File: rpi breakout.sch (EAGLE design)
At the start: 48 parts, among them IC1 PCA9505, J1 RASPBERRYPI-40-PIN-GPIO_PTH, U1 MAX11642EEG, U2 MAX11642EEG, U3 MAX11642EEG

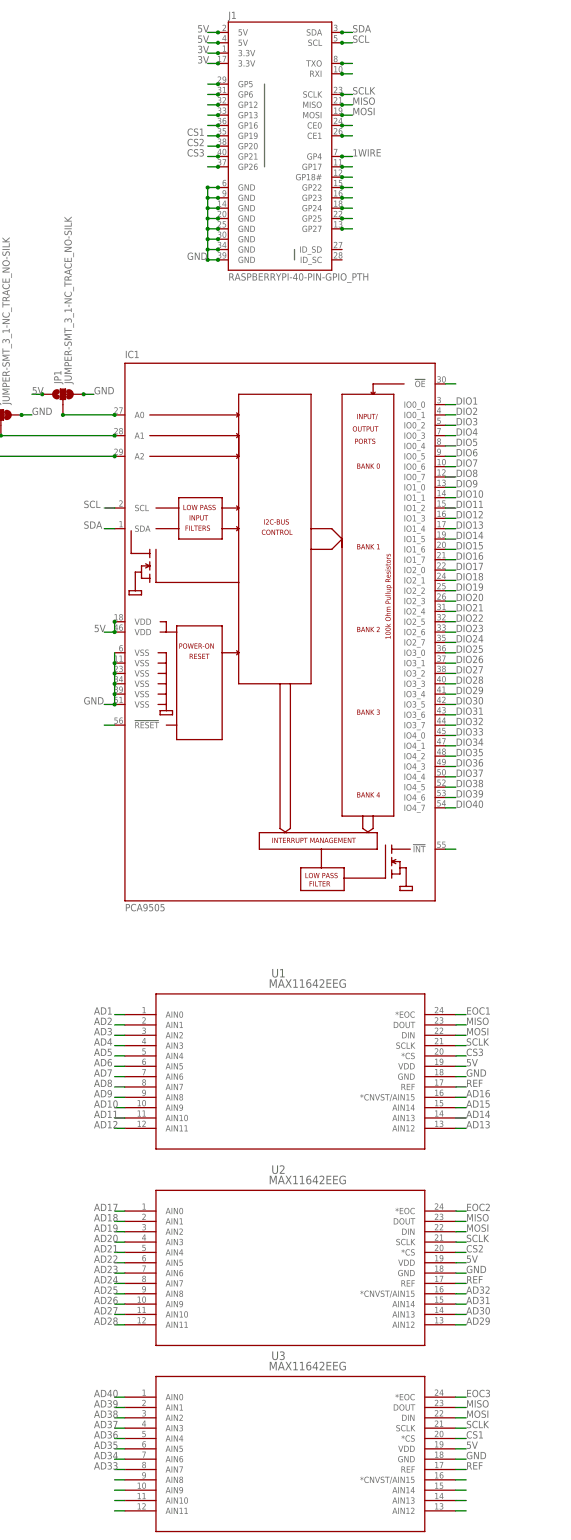
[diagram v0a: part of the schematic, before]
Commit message: FInal routing pass
connected remaining pins, added decoupling caps to AREF pins.
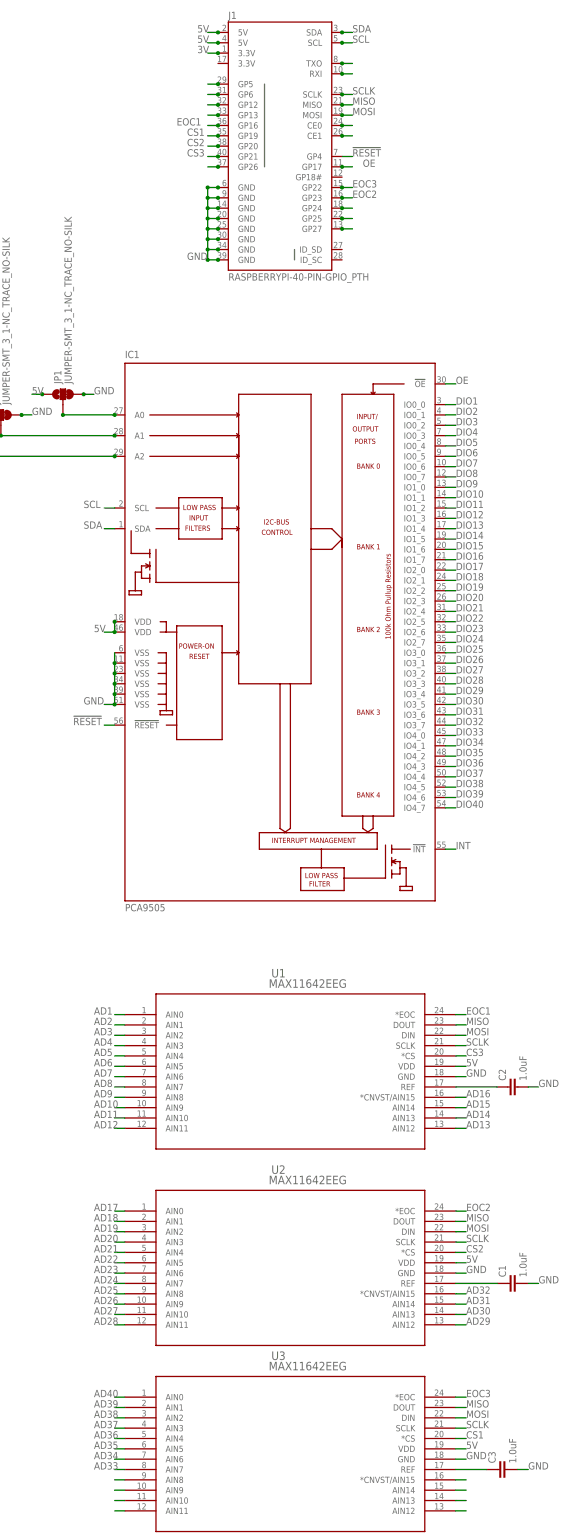
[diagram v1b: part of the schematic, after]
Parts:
- added C1, C2, C3: 1.0uF, SparkFun-Capacitors:1.0UF-0805-25V-10%
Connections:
- net N$14 renamed INT
- removed net 1WIRE: J1.GP4
- removed net N$1: IC1.!RESET
- removed net N$15: IC1.!OE
- removed net N$32: J1.GP17
- removed net N$33: J1.GP18#
- removed net N$34: J1.GP22
- removed net N$35: J1.GP23
- removed net N$9: J1.GP16
- removed net REF: U1.REF, U2.REF, U3.REF
- new net !RESET: IC1.!RESET, J1.GP4
- new net N$11: C2.1, U1.REF
- new net N$2: C3.1, U3.REF
- new net N$3: C1.1, U2.REF
- new net OE: IC1.!OE, J1.GP17
- net 3V: no longer J1.3.3V@17
- net EOC1: now also J1.GP16
- net EOC2: now also J1.GP23
- net EOC3: now also J1.GP22
- net GND: now also C1.2, C2.2, C3.2
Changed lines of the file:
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@@
 <part name="JP2" library="SparkFun-Jumpers" library_urn="urn:adsk.eagle:library:528" deviceset="JUMPER-SMT_3_1-NC_TRACE" device="_NO-SILK" package3d_urn="urn:adsk.eagle:package:39287/1"/>
 <part name="JP3" library="SparkFun-Jumpers" library_urn="urn:adsk.eagle:library:528" deviceset="JUMPER-SMT_3_1-NC_TRACE" device="_NO-SILK" package3d_urn="urn:adsk.eagle:package:39287/1"/>
+<part name="C1" library="SparkFun-Capacitors" library_urn="urn:adsk.eagle:library:510" deviceset="1.0UF" device="-0805-25V-10%" package3d_urn="urn:adsk.eagle:package:37429/1" value="1.0uF"/>
+<part name="C2" library="SparkFun-Capacitors" library_urn="urn:adsk.eagle:library:510" deviceset="1.0UF" device="-0805-25V-10%" package3d_urn="urn:adsk.eagle:package:37429/1" value="1.0uF"/>
+<part name="C3" library="SparkFun-Capacitors" library_urn="urn:adsk.eagle:library:510" deviceset="1.0UF" device="-0805-25V-10%" package3d_urn="urn:adsk.eagle:package:37429/1" value="1.0uF"/>
 </parts>
 <sheets>
@@
 <attribute name="VALUE" x="175.641" y="83.82" size="1.778" layer="96" font="vector" rot="R90" align="top-left"/>
 </instance>
+<instance part="C1" gate="G$1" x="317.5" y="-127" smashed="yes" rot="R90">
+<attribute name="NAME" x="314.579" y="-125.476" size="1.778" layer="95" font="vector" rot="R90"/>
+<attribute name="VALUE" x="319.659" y="-125.476" size="1.778" layer="96" font="vector" rot="R90"/>
+</instance>
+<instance part="C2" gate="G$1" x="317.5" y="-78.74" smashed="yes" rot="R90">
+<attribute name="NAME" x="314.579" y="-77.216" size="1.778" layer="95" font="vector" rot="R90"/>
+<attribute name="VALUE" x="319.659" y="-77.216" size="1.778" layer="96" font="vector" rot="R90"/>
+</instance>
+<instance part="C3" gate="G$1" x="314.96" y="-172.72" smashed="yes" rot="R90">
+<attribute name="NAME" x="312.039" y="-171.196" size="1.778" layer="95" font="vector" rot="R90"/>
+<attribute name="VALUE" x="317.119" y="-171.196" size="1.778" layer="96" font="vector" rot="R90"/>
+</instance>
 </instances>
 <busses>
@@
 </segment>
 </net>
-<net name="N$9" class="0">
-<segment>
-<pinref part="J1" gate="G$1" pin="GP16"/>
-<wire x1="243.84" y1="157.48" x2="241.3" y2="157.48" width="0.1524" layer="91"/>
-<junction x="243.84" y="157.48"/>
-</segment>
-</net>
 <net name="N$13" class="0">
 <segment>
@@
 </segment>
 </net>
-<net name="N$32" class="0">
-<segment>
-<pinref part="J1" gate="G$1" pin="GP17"/>
-<wire x1="274.32" y1="147.32" x2="276.86" y2="147.32" width="0.1524" layer="91"/>
-<junction x="274.32" y="147.32"/>
-</segment>
-</net>
-<net name="N$33" class="0">
-<segment>
-<pinref part="J1" gate="G$1" pin="GP18#"/>
-<wire x1="274.32" y1="144.78" x2="276.86" y2="144.78" width="0.1524" layer="91"/>
-<junction x="274.32" y="144.78"/>
-</segment>
-</net>
-<net name="N$34" class="0">
-<segment>
-<pinref part="J1" gate="G$1" pin="GP22"/>
-<wire x1="274.32" y1="142.24" x2="276.86" y2="142.24" width="0.1524" layer="91"/>
-<junction x="274.32" y="142.24"/>
-</segment>
-</net>
-<net name="N$35" class="0">
-<segment>
-<pinref part="J1" gate="G$1" pin="GP23"/>
-<wire x1="274.32" y1="139.7" x2="276.86" y2="139.7" width="0.1524" layer="91"/>
-<junction x="274.32" y="139.7"/>
-</segment>
-</net>
 <net name="N$36" class="0">
 <segment>
@@
 <junction x="243.84" y="175.26"/>
 <label x="238.76" y="175.26" size="1.778" layer="95"/>
-</segment>
-<segment>
-<pinref part="J1" gate="G$1" pin="3.3V@17"/>
-<wire x1="243.84" y1="172.72" x2="241.3" y2="172.72" width="0.1524" layer="91"/>
-<junction x="243.84" y="172.72"/>
-<label x="238.76" y="172.72" size="1.778" layer="95"/>
-</segment>
-</net>
-<net name="1WIRE" class="0">
-<segment>
-<pinref part="J1" gate="G$1" pin="GP4"/>
-<wire x1="274.32" y1="149.86" x2="276.86" y2="149.86" width="0.1524" layer="91"/>
-<junction x="274.32" y="149.86"/>
-<label x="276.86" y="149.86" size="1.778" layer="95"/>
 </segment>
 </net>
@@
 <junction x="180.34" y="81.28"/>
 </segment>
+<segment>
+<pinref part="C2" gate="G$1" pin="2"/>
+<wire x1="320.04" y1="-78.74" x2="322.58" y2="-78.74" width="0.1524" layer="91"/>
+<label x="322.58" y="-78.74" size="1.778" layer="95"/>
+</segment>
+<segment>
+<pinref part="C1" gate="G$1" pin="2"/>
+<wire x1="320.04" y1="-127" x2="322.58" y2="-127" width="0.1524" layer="91"/>
+<label x="322.58" y="-127" size="1.778" layer="95"/>
+</segment>
+<segment>
+<pinref part="C3" gate="G$1" pin="2"/>
+<wire x1="317.5" y1="-172.72" x2="320.04" y2="-172.72" width="0.1524" layer="91"/>
+<label x="320.04" y="-172.72" size="1.778" layer="95"/>
+</segment>
 </net>
 <net name="5V" class="0">
@@
 </segment>
 </net>
-<net name="N$1" class="0">
+<net name="!RESET" class="0">
 <segment>
 <pinref part="IC1" gate="G$1" pin="!RESET"/>
 <wire x1="218.44" y1="10.16" x2="215.9" y2="10.16" width="0.1524" layer="91"/>
-</segment>
-</net>
-<net name="N$14" class="0">
+<label x="208.28" y="10.16" size="1.778" layer="95"/>
+</segment>
+<segment>
+<pinref part="J1" gate="G$1" pin="GP4"/>
+<wire x1="274.32" y1="149.86" x2="276.86" y2="149.86" width="0.1524" layer="91"/>
+<label x="276.86" y="149.86" size="1.778" layer="95"/>
+</segment>
+</net>
+<net name="INT" class="0">
 <segment>
 <pinref part="IC1" gate="G$1" pin="!INT"/>
 <wire x1="299.72" y1="-20.32" x2="302.26" y2="-20.32" width="0.1524" layer="91"/>
-</segment>
-</net>
-<net name="N$15" class="0">
+<label x="302.26" y="-20.32" size="1.778" layer="95"/>
+</segment>
+</net>
+<net name="OE" class="0">
 <segment>
 <pinref part="IC1" gate="G$1" pin="!OE"/>
 <wire x1="299.72" y1="93.98" x2="302.26" y2="93.98" width="0.1524" layer="91"/>
+<label x="302.26" y="93.98" size="1.778" layer="95"/>
+</segment>
+<segment>
+<pinref part="J1" gate="G$1" pin="GP17"/>
+<wire x1="274.32" y1="147.32" x2="276.86" y2="147.32" width="0.1524" layer="91"/>
+<junction x="274.32" y="147.32"/>
+<label x="279.4" y="147.32" size="1.778" layer="95"/>
 </segment>
 </net>
@@
 </segment>
 </net>
-<net name="REF" class="0">
-<segment>
-<pinref part="U1" gate="A" pin="REF"/>
-<wire x1="302.26" y1="-78.74" x2="304.8" y2="-78.74" width="0.1524" layer="91"/>
-<label x="304.8" y="-78.74" size="1.778" layer="95"/>
-</segment>
-<segment>
-<pinref part="U2" gate="A" pin="REF"/>
-<wire x1="302.26" y1="-127" x2="304.8" y2="-127" width="0.1524" layer="91"/>
-<label x="304.8" y="-127" size="1.778" layer="95"/>
-</segment>
-<segment>
-<pinref part="U3" gate="A" pin="REF"/>
-<wire x1="302.26" y1="-172.72" x2="304.8" y2="-172.72" width="0.1524" layer="91"/>
-<label x="304.8" y="-172.72" size="1.778" layer="95"/>
-</segment>
-</net>
 <net name="EOC1" class="0">
 <segment>
@@
 <label x="304.8" y="-60.96" size="1.778" layer="95"/>
 </segment>
+<segment>
+<pinref part="J1" gate="G$1" pin="GP16"/>
+<wire x1="243.84" y1="157.48" x2="241.3" y2="157.48" width="0.1524" layer="91"/>
+<junction x="243.84" y="157.48"/>
+<label x="233.68" y="157.48" size="1.778" layer="95"/>
+</segment>
 </net>
 <net name="EOC2" class="0">
@@
 <wire x1="302.26" y1="-109.22" x2="304.8" y2="-109.22" width="0.1524" layer="91"/>
 <label x="304.8" y="-109.22" size="1.778" layer="95"/>
+</segment>
+<segment>
+<pinref part="J1" gate="G$1" pin="GP23"/>
+<wire x1="274.32" y1="139.7" x2="276.86" y2="139.7" width="0.1524" layer="91"/>
+<junction x="274.32" y="139.7"/>
+<label x="276.86" y="139.7" size="1.778" layer="95"/>
 </segment>
 </net>
@@
 <label x="304.8" y="-154.94" size="1.778" layer="95"/>
 </segment>
+<segment>
+<pinref part="J1" gate="G$1" pin="GP22"/>
+<wire x1="274.32" y1="142.24" x2="276.86" y2="142.24" width="0.1524" layer="91"/>
+<junction x="274.32" y="142.24"/>
+<label x="276.86" y="142.24" size="1.778" layer="95"/>
+</segment>
 </net>
 <net name="CS3" class="0">
@@
 </segment>
 </net>
+<net name="N$2" class="0">
+<segment>
+<pinref part="U3" gate="A" pin="REF"/>
+<pinref part="C3" gate="G$1" pin="1"/>
+<wire x1="302.26" y1="-172.72" x2="309.88" y2="-172.72" width="0.1524" layer="91"/>
+</segment>
+</net>
+<net name="N$3" class="0">
+<segment>
+<pinref part="U2" gate="A" pin="REF"/>
+<pinref part="C1" gate="G$1" pin="1"/>
+<wire x1="302.26" y1="-127" x2="312.42" y2="-127" width="0.1524" layer="91"/>
+</segment>
+</net>
+<net name="N$11" class="0">
+<segment>
+<pinref part="U1" gate="A" pin="REF"/>
+<pinref part="C2" gate="G$1" pin="1"/>
+<wire x1="302.26" y1="-78.74" x2="312.42" y2="-78.74" width="0.1524" layer="91"/>
+</segment>
+</net>

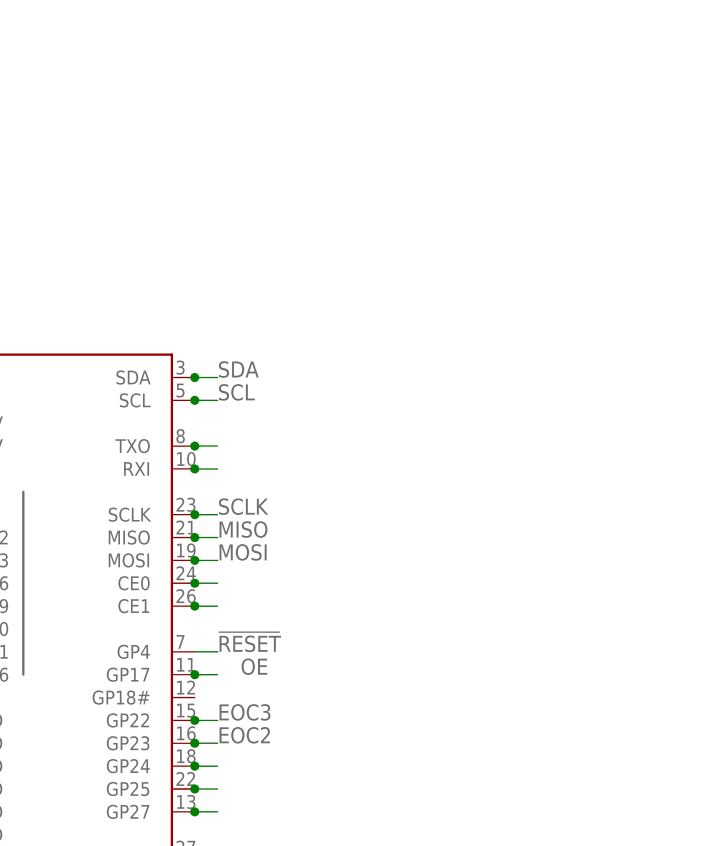
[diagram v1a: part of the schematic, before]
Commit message: pulled OE and Reset lines to 5v and ground
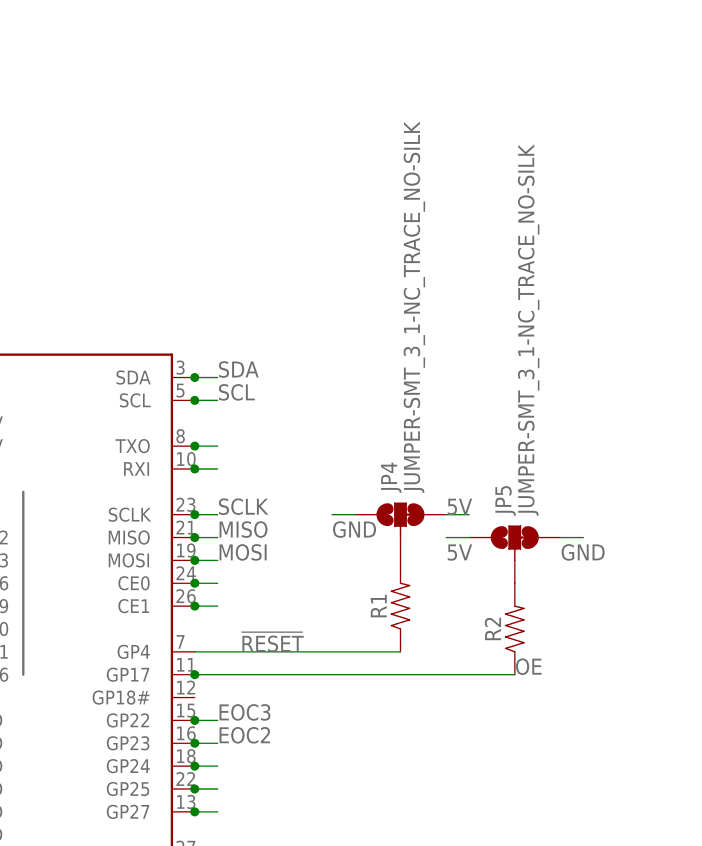
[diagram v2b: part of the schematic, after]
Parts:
- added JP4, JP5: JUMPER-SMT_3_1-NC_TRACE_NO-SILK, SparkFun-Jumpers:JUMPER-SMT_3_1-NC_TRACE_NO-SILK
- added R1, R2: (no value), SparkFun-Resistors:RESISTOR0805
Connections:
- new net N$1: JP4.2, R1.2
- new net N$4: JP5.2, R2.2
- net !RESET: now also R1.1
- net 5V: now also JP4.3, JP5.1
- net GND: now also JP4.1, JP5.3
- net OE: now also R2.1
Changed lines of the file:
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@@
 <part name="C2" library="SparkFun-Capacitors" library_urn="urn:adsk.eagle:library:510" deviceset="1.0UF" device="-0805-25V-10%" package3d_urn="urn:adsk.eagle:package:37429/1" value="1.0uF"/>
 <part name="C3" library="SparkFun-Capacitors" library_urn="urn:adsk.eagle:library:510" deviceset="1.0UF" device="-0805-25V-10%" package3d_urn="urn:adsk.eagle:package:37429/1" value="1.0uF"/>
+<part name="R1" library="SparkFun-Resistors" library_urn="urn:adsk.eagle:library:532" deviceset="RESISTOR" device="0805" package3d_urn="urn:adsk.eagle:package:39651/1" value=" "/>
+<part name="R2" library="SparkFun-Resistors" library_urn="urn:adsk.eagle:library:532" deviceset="RESISTOR" device="0805" package3d_urn="urn:adsk.eagle:package:39651/1" value=" "/>
+<part name="JP4" library="SparkFun-Jumpers" library_urn="urn:adsk.eagle:library:528" deviceset="JUMPER-SMT_3_1-NC_TRACE" device="_NO-SILK" package3d_urn="urn:adsk.eagle:package:39287/1"/>
+<part name="JP5" library="SparkFun-Jumpers" library_urn="urn:adsk.eagle:library:528" deviceset="JUMPER-SMT_3_1-NC_TRACE" device="_NO-SILK" package3d_urn="urn:adsk.eagle:package:39287/1"/>
 </parts>
 <sheets>
@@
 <attribute name="NAME" x="312.039" y="-171.196" size="1.778" layer="95" font="vector" rot="R90"/>
 <attribute name="VALUE" x="317.119" y="-171.196" size="1.778" layer="96" font="vector" rot="R90"/>
+</instance>
+<instance part="R1" gate="G$1" x="297.18" y="154.94" smashed="yes" rot="R90">
+<attribute name="NAME" x="295.656" y="154.94" size="1.778" layer="95" font="vector" rot="R90" align="bottom-center"/>
+<attribute name="VALUE" x="298.704" y="154.94" size="1.778" layer="96" font="vector" rot="R90" align="top-center"/>
+</instance>
+<instance part="R2" gate="G$1" x="309.88" y="152.4" smashed="yes" rot="R90">
+<attribute name="NAME" x="308.356" y="152.4" size="1.778" layer="95" font="vector" rot="R90" align="bottom-center"/>
+<attribute name="VALUE" x="311.404" y="152.4" size="1.778" layer="96" font="vector" rot="R90" align="top-center"/>
+</instance>
+<instance part="JP4" gate="G$1" x="297.18" y="165.1" smashed="yes" rot="R90">
+<attribute name="NAME" x="296.799" y="167.64" size="1.778" layer="95" font="vector" rot="R90"/>
+<attribute name="VALUE" x="297.561" y="167.64" size="1.778" layer="96" font="vector" rot="R90" align="top-left"/>
+</instance>
+<instance part="JP5" gate="G$1" x="309.88" y="162.56" smashed="yes" rot="R90">
+<attribute name="NAME" x="309.499" y="165.1" size="1.778" layer="95" font="vector" rot="R90"/>
+<attribute name="VALUE" x="310.261" y="165.1" size="1.778" layer="96" font="vector" rot="R90" align="top-left"/>
 </instance>
 </instances>
@@
 <label x="320.04" y="-172.72" size="1.778" layer="95"/>
 </segment>
+<segment>
+<pinref part="JP5" gate="G$1" pin="3"/>
+<wire x1="314.96" y1="162.56" x2="317.5" y2="162.56" width="0.1524" layer="91"/>
+<label x="314.96" y="160.02" size="1.778" layer="95"/>
+</segment>
+<segment>
+<pinref part="JP4" gate="G$1" pin="1"/>
+<wire x1="292.1" y1="165.1" x2="289.56" y2="165.1" width="0.1524" layer="91"/>
+<label x="289.56" y="162.56" size="1.778" layer="95"/>
+</segment>
 </net>
 <net name="5V" class="0">
@@
 <junction x="200.66" y="91.44"/>
 </segment>
+<segment>
+<pinref part="JP4" gate="G$1" pin="3"/>
+<wire x1="302.26" y1="165.1" x2="304.8" y2="165.1" width="0.1524" layer="91"/>
+<label x="302.26" y="165.1" size="1.778" layer="95"/>
+</segment>
+<segment>
+<pinref part="JP5" gate="G$1" pin="1"/>
+<wire x1="304.8" y1="162.56" x2="302.26" y2="162.56" width="0.1524" layer="91"/>
+<label x="302.26" y="160.02" size="1.778" layer="95"/>
+</segment>
 </net>
 <net name="SDA" class="0">
@@
 <segment>
 <pinref part="J1" gate="G$1" pin="GP4"/>
-<wire x1="274.32" y1="149.86" x2="276.86" y2="149.86" width="0.1524" layer="91"/>
-<label x="276.86" y="149.86" size="1.778" layer="95"/>
+<wire x1="274.32" y1="149.86" x2="297.18" y2="149.86" width="0.1524" layer="91"/>
+<label x="279.4" y="149.86" size="1.778" layer="95"/>
+<pinref part="R1" gate="G$1" pin="1"/>
 </segment>
 </net>
@@
 <segment>
 <pinref part="J1" gate="G$1" pin="GP17"/>
-<wire x1="274.32" y1="147.32" x2="276.86" y2="147.32" width="0.1524" layer="91"/>
+<wire x1="274.32" y1="147.32" x2="309.88" y2="147.32" width="0.1524" layer="91"/>
 <junction x="274.32" y="147.32"/>
-<label x="279.4" y="147.32" size="1.778" layer="95"/>
+<label x="309.88" y="147.32" size="1.778" layer="95"/>
+<pinref part="R2" gate="G$1" pin="1"/>
 </segment>
 </net>
@@
 </segment>
 </net>
+<net name="N$1" class="0">
+<segment>
+<pinref part="R1" gate="G$1" pin="2"/>
+<pinref part="JP4" gate="G$1" pin="2"/>
+</segment>
+</net>
+<net name="N$4" class="0">
+<segment>
+<pinref part="R2" gate="G$1" pin="2"/>
+<pinref part="JP5" gate="G$1" pin="2"/>
+</segment>
+</net>
